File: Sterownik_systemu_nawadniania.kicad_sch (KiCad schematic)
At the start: 19 parts

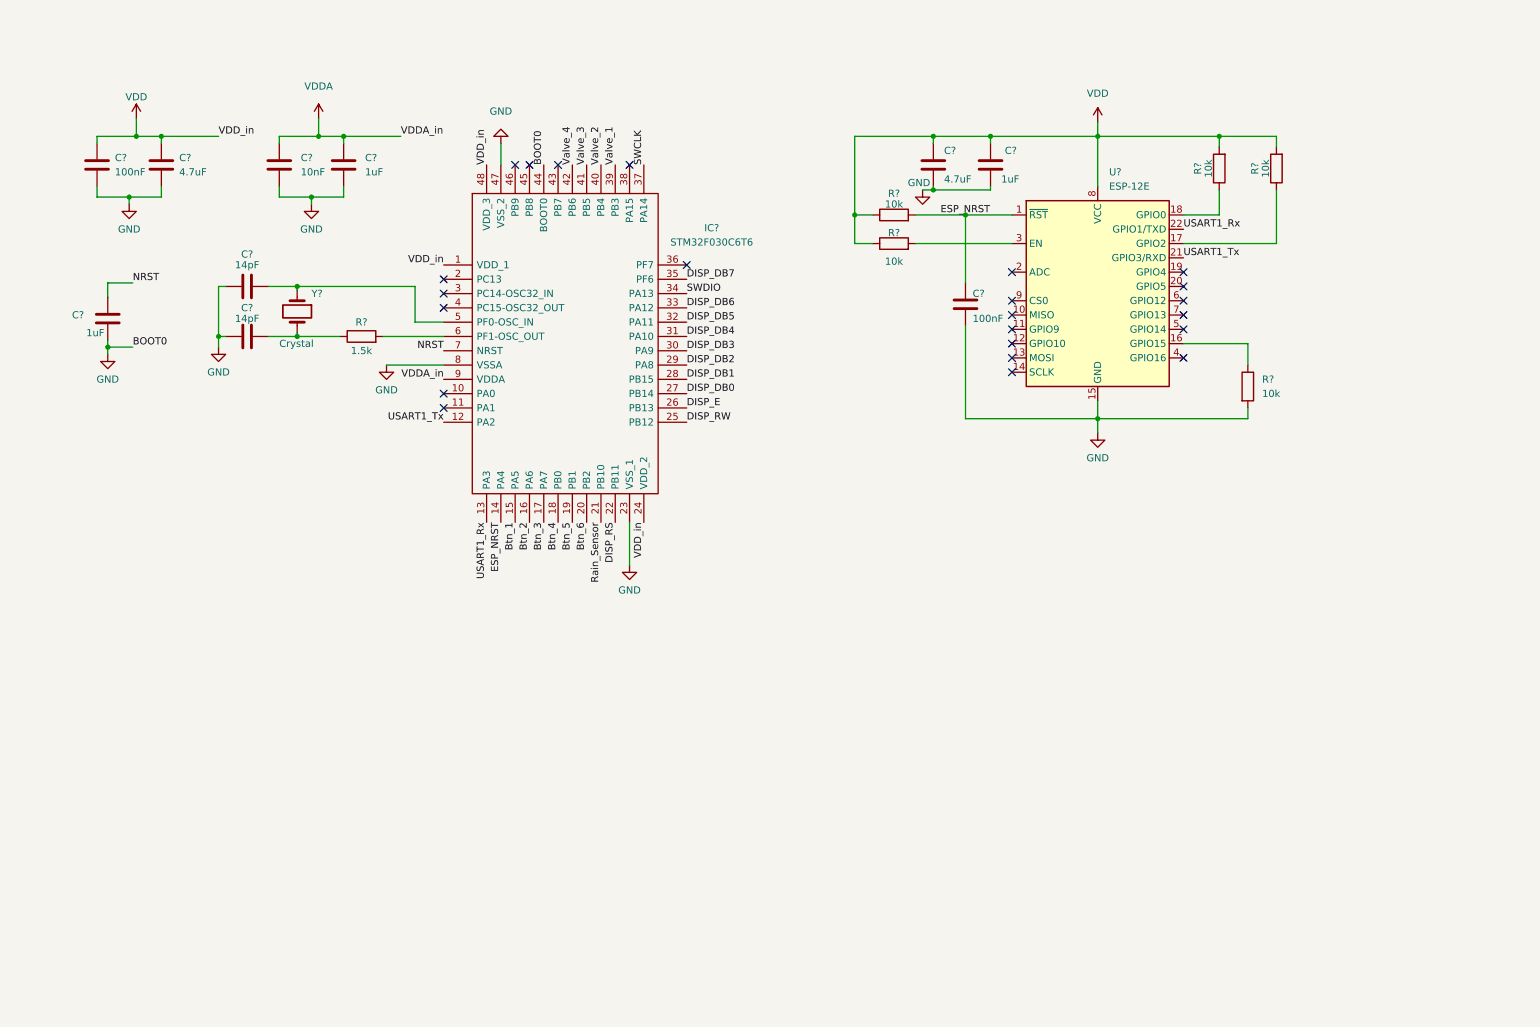
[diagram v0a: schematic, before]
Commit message: 6 buttons with RC filters
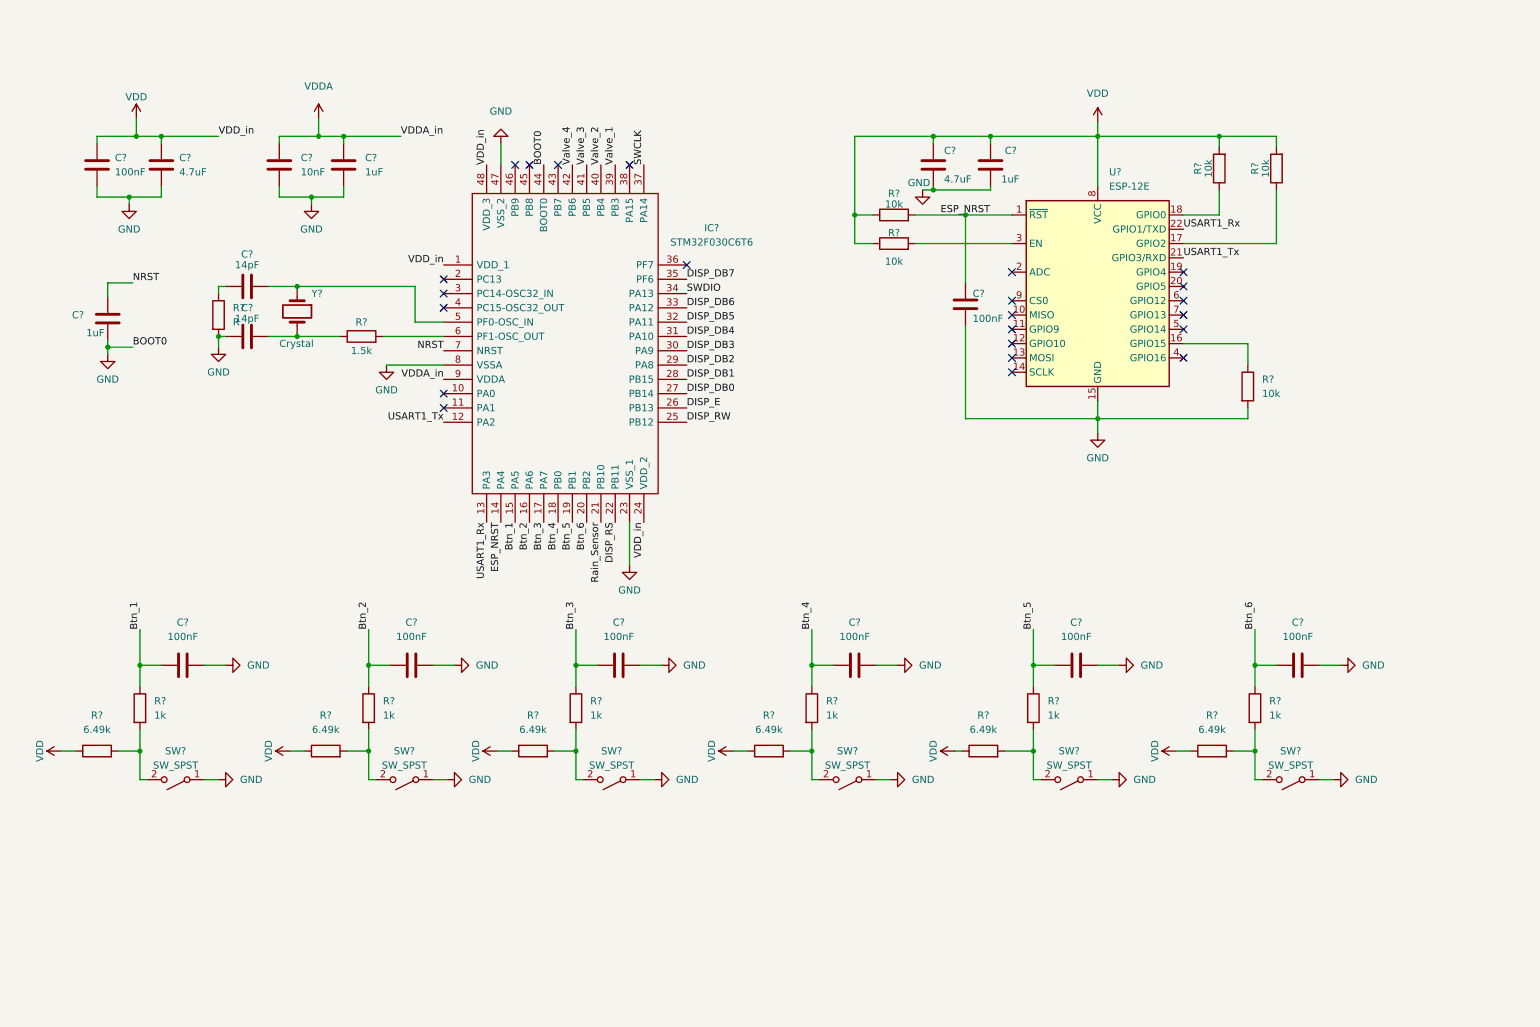
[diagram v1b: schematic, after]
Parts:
- added C? (x6): 100nF, symbol Device:C
- added R? (x6): 6.49k, symbol Device:R
- added R?: R, symbol Device:R
- added R? (x6): 1k, symbol Device:R
- added SW? (x6): SW_SPST, symbol Switch:SW_SPST
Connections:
- net Btn_1: now also C?.1, R?.1
- net Btn_2: now also C?.1, R?.1
- net Btn_3: now also C?.1, R?.1
- net Btn_4: now also C?.1, R?.1
- net Btn_5: now also C?.1, R?.1
- net Btn_6: now also C?.1, R?.1
- net GND: now also C?.2, C?.2, C?.2, C?.2, C?.2, C?.2, R?.2, SW?.1 (A), SW?.1 (A), SW?.1 (A), SW?.1 (A), SW?.1 (A), SW?.1 (A); no longer C?.1
- net VDD: now also R?.1, R?.1, R?.1, R?.1, R?.1, R?.1
- new net: R?.2, R?.2, SW?.2 (B) (x6)
- new net: C?.1, R?.1

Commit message: power unit
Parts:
- added C?: 1uF, symbol Device:C
- added C? (x2): 22uF, symbol Device:C
- added C? (x2): 100nF, symbol Device:C
- added J?: Conn_01x05_Male, symbol Connector:Conn_01x05_Male
- added J?: CON-SOCJ-2155, GRAVITECH_CON-SOCJ-2155, symbol CON-SOCJ-2155:CON-SOCJ-2155
- added J?: Conn_01x16_Female, symbol Connector:Conn_01x16_Female
- added L?: 12uH, symbol Device:L
- added R?: 100, symbol Device:R
- added R?: 51k, symbol Device:R
- added R?: 22.1k, symbol Device:R
- added RV?: R_Potentiometer, symbol Device:R_Potentiometer
- added SW?: 25336NA, Apem_Inc.-25336NA-*, symbol eec2:25336NA
- added U?: LMR50410XDBVR, Texas_Instruments-DBV0006A-0-0-*, symbol eec:LMR50410XDBVR
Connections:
- net DISP_DB0: now also J?.7 (Pin_7)
- net DISP_DB1: now also J?.8 (Pin_8)
- net DISP_DB2: now also J?.9 (Pin_9)
- net DISP_DB3: now also J?.10 (Pin_10)
- net DISP_DB4: now also J?.11 (Pin_11)
- net DISP_DB5: now also J?.12 (Pin_12)
- net DISP_DB6: now also J?.13 (Pin_13)
- net DISP_DB7: now also J?.14 (Pin_14)
- net DISP_E: now also J?.6 (Pin_6)
- net DISP_RS: now also J?.4 (Pin_4)
- net DISP_RW: now also J?.5 (Pin_5)
- net GND: now also C?.2, C?.2, C?.2, C?.2, J?.1 (Pin_1), J?.16 (Pin_16), J?.2, J?.3, J?.4 (Pin_4), R?.2, RV?.3, U?.2 (GND)
- net NRST: now also J?.1 (Pin_1)
- net SWCLK: now also J?.2 (Pin_2)
- net SWDIO: now also J?.3 (Pin_3)
- net VDD: now also C?.1, C?.1, J?.2 (Pin_2), J?.5 (Pin_5), L?.2, R?.1, R?.1, RV?.1
- new net: J?.15 (Pin_15), R?.2
- new net: C?.1, L?.1, U?.1 (CB)
- new net: R?.1, R?.2, U?.3 (FB)
- new net: C?.2, U?.6 (SW)
- new net: J?.1, SW?.3 (Common)
- new net 24V: C?.1, C?.1, SW?.1, U?.4 (EN), U?.5 (VIN)
- new net DISP_Contrast: J?.3 (Pin_3), RV?.2
- no-connect marks 23 -> 24
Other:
- added sheet Relays_and_sensor (Relays_and_sensor.kicad_sch)
- note added: "Buttons connection"
- note added: "Connectors"
- note added: "ESP-12E"
- note added: "MCU"
- note added: "PSU"
- note added: "Power Flags"
- note added: "Realys and sensor"
- moved on the sheet: C?, IC?, R?, SW?, U?, Y?

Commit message: Rain sensor
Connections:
- net Rain_Sensor: no longer IC?.21 (PB10)
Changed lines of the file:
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@@
-    (effects (font (size 1.27 1.27)) (justify right bottom))
-  )
-  (label "Rain_Sensor" (at 107.95 93.345 270)
     (effects (font (size 1.27 1.27)) (justify right bottom))
   )
@@
   (label "DISP_DB2" (at 123.19 65.405 0)
     (effects (font (size 1.27 1.27)) (justify left bottom))
+  )
+  (global_label "Rain_Sensor" (shape input) (at 106.68 92.71 270) (fields_autoplaced)
+    (effects (font (size 1.27 1.27)) (justify right))
+    (property "Intersheet References" "${INTERSHEET_REFS}" (id 0) (at 106.6006 106.6741 90)
+      (effects (font (size 1.27 1.27)) (justify right) hide)
+    )
   )
   (symbol (lib_id "power:GND") (at 69.85 65.405 0) (unit 1)
@@
       (reference "#PWR?") (unit 1) (value "GND") (footprint "")
     )
+    (path "/40474f4f-d3ba-4b7e-8552-7edd7400a511/02e4c25a-6000-402f-864b-7d88ccb35804"
+      (reference "#PWR?") (unit 1) (value "VDD") (footprint "")
+    )
     (path "/0840e0a5-9e4a-4831-b6d7-41f10b84a503"
       (reference "#PWR?") (unit 1) (value "GND") (footprint "")
@@
       (reference "#PWR?") (unit 1) (value "VDDA") (footprint "")
     )
+    (path "/40474f4f-d3ba-4b7e-8552-7edd7400a511/4aea0a1c-cd4e-48c9-a8b2-37d7047cf61d"
+      (reference "#PWR?") (unit 1) (value "GND") (footprint "")
+    )
     (path "/64c354c8-543f-4b77-a390-22f8fc9aa39e"
       (reference "#PWR?") (unit 1) (value "GND") (footprint "")
@@
       (reference "#PWR?") (unit 1) (value "VDD") (footprint "")
     )
+    (path "/40474f4f-d3ba-4b7e-8552-7edd7400a511/95356824-109f-4a8b-b778-1aa84bcc6c4e"
+      (reference "#PWR?") (unit 1) (value "GND") (footprint "")
+    )
     (path "/98dc4df6-1474-443f-8f1f-ccaabe997497"
       (reference "#PWR?") (unit 1) (value "GND") (footprint "")
@@
       (reference "C?") (unit 1) (value "14pF") (footprint "")
     )
+    (path "/40474f4f-d3ba-4b7e-8552-7edd7400a511/a0547789-3aa4-4065-bc42-13d1ca692086"
+      (reference "C?") (unit 1) (value "100nF") (footprint "")
+    )
     (path "/cfabea6e-e7c5-4b61-8fa2-06fea7bb845f"
       (reference "C?") (unit 1) (value "100nF") (footprint "")
@@
       (reference "J?") (unit 1) (value "Conn_01x16_Female") (footprint "")
     )
+    (path "/40474f4f-d3ba-4b7e-8552-7edd7400a511/e8cc52bd-a0a0-4335-bca6-e98c2202191a"
+      (reference "J?") (unit 1) (value "Screw_Terminal_01x02") (footprint "")
+    )
     (path "/2e838c8d-b3cf-4c8c-b320-ce77ae7c40ce"
       (reference "L?") (unit 1) (value "12uH") (footprint "")
@@
       (reference "R?") (unit 1) (value "100") (footprint "")
     )
+    (path "/40474f4f-d3ba-4b7e-8552-7edd7400a511/1f968d70-6bc6-4606-bf7c-a3dcd0b13741"
+      (reference "R?") (unit 1) (value "6.49k") (footprint "")
+    )
     (path "/34a2c40f-7d29-4705-9cda-64f123add787"
       (reference "R?") (unit 1) (value "1.5k") (footprint "")
@@
       (reference "R?") (unit 1) (value "1k") (footprint "")
     )
+    (path "/40474f4f-d3ba-4b7e-8552-7edd7400a511/ae3ebb40-0432-4183-9cc5-d890c53c3a6d"
+      (reference "R?") (unit 1) (value "1k") (footprint "")
+    )

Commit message: ver 0.1
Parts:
- gave numbers to parts that had none: 59
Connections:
- net Rain_sensor: now reaches IC1.21 (PB10)
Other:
- sheet Relays_and_sensor ports: added 24V, Rain_sensor, Valve_1, Valve_2, Valve_3, Valve_4; removed none

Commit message: Lab 07.11
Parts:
- removed R5: R, symbol Device:R
- R1, R11, R12, R2, R7, R8: value 6.49k -> 10k
- R22: Purpose (none) -> TBD
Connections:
- net VDDA is gone; now on net VDD: C8.1, C9.1, IC1.9 (VDDA)
- net GND: now also C6.1
- net 24V renamed +24V
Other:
- sheet Relays_and_sensor ports: added none; removed 24V

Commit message: Rezystory, kondensatory, cewka - footprints
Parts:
- C1, C10, C11, C12, C13, C14, C15, C16, C17, C18, C19, C2, C3, C4, C5, C8, C9: footprint (none) -> Capacitor_SMD:C_0603_1608Metric
- C20, C21: footprint (none) -> Capacitor_SMD:C_2220_5650Metric
- C6, C7: footprint (none) -> Capacitor_SMD:C_0402_1005Metric
- IC1: footprint QFP50P900X900X160-48N -> (none)
- J1: footprint GRAVITECH_CON-SOCJ-2155 -> (none)
- L1: footprint (none) -> ul_RLB0712-120KL:RLB0712-120KL
- R1, R10, R11, R12, R13, R14, R15, R16, R17, R18, R19, R2, R20, R21, R22, R3, R4, R6, R7, R8, R9: footprint (none) -> Resistor_SMD:R_0603_1608Metric
- SW7: footprint Apem_Inc.-25336NA-* -> (none)
- U2: footprint Texas_Instruments-DBV0006A-0-0-* -> (none)

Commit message: footprints
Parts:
- IC1: footprint (none) -> STM32F030:QFP50P900X900X160-48N
- J1: footprint (none) -> CON-SOCJ-2155:GRAVITECH_CON-SOCJ-2155
- J2: footprint (none) -> Connector_PinHeader_2.54mm:PinHeader_1x05_P2.54mm_Vertical
- J3: footprint (none) -> Connector_PinSocket_2.54mm:PinSocket_1x16_P2.54mm_Vertical
- RV1: value R_Potentiometer -> 10k; footprint (none) -> 3362P-1-103LF:TRIM_3362P-1-103LF
- SW1, SW2, SW3, SW4, SW5, SW6: footprint (none) -> Project_lic_footprints_AM:430156043736_AM
- SW7: footprint (none) -> eec3:Apem_Inc.-25336NA-MFG
- U2: footprint (none) -> eec2:Texas_Instruments-DBV0006A-0-0-MFG
- Y1: footprint (none) -> ECS-80-12-30Q-DS-TR:XTAL_ECS-80-18-30-JGN-TR; Purpose (none) -> ECS-80-12-30Q-DS-TR
